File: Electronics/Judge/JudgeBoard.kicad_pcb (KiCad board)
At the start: 2 copper layers, 17 parts, among them J1 RJ12-UNSHLD, U1 74HC165, U2 74HC165

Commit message: UPdated judge board layout
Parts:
- S1: value DPDT-Button -> R1
- S10: value DPDT-Button -> B5
- S2: value DPDT-Button -> R3
- S3: value DPDT-Button -> R5
- S4: value DPDT-Button -> B2
- S5: value DPDT-Button -> B4
- S6: value DPDT-Button -> R2
- S7: value DPDT-Button -> R4
- S8: value DPDT-Button -> B1
- S9: value DPDT-Button -> B3
- moved S6 97.7 mm to (58.9, 81.8)
- moved S7 95.5 mm to (58.4, 115.3)
- moved S4 94.6 mm to (143.3, 81.3)
- moved S5 92.5 mm to (145.8, 115.3)
- moved S9 52.7 mm to (149.4, 95.0)
- moved S1 50.9 mm to (51.3, 105.7)
- moved S2 49.8 mm to (45.2, 96.0)
- moved U2 47.1 mm to (124.5, 106.2), turned to 270 degrees
- moved RN1 42.7 mm to (79.8, 119.9), turned to 0 degrees
- moved S3 30.5 mm to (55.9, 95.0)
- moved S8 29.3 mm to (141.7, 105.2)
- moved S10 23.2 mm to (135.6, 95.0)
- moved J1 14.5 mm to (96.5, 81.3)
- moved C1 10.8 mm to (73.7, 110.7), turned to 90 degrees
- moved C2 9.16 mm to (101.6, 110.7), turned to 90 degrees
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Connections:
- J1 pad 5: Net-(J1-Pad5) -> (no net)
- S1 pad 3: Net-(S1-Pad3) -> (no net)
- S1 pad 4: Net-(S1-Pad4) -> (no net)
- S1 pad 5: Net-(S1-Pad5) -> (no net)
- S1 pad 6: Net-(S1-Pad6) -> (no net)
- S10 pad 3: Net-(S10-Pad3) -> (no net)
- S10 pad 4: Net-(S10-Pad4) -> (no net)
- S10 pad 5: Net-(S10-Pad5) -> (no net)
- S10 pad 6: Net-(S10-Pad6) -> (no net)
- S2 pad 3: Net-(S2-Pad3) -> (no net)
- S2 pad 4: Net-(S2-Pad4) -> (no net)
- S2 pad 5: Net-(S2-Pad5) -> (no net)
- S2 pad 6: Net-(S2-Pad6) -> (no net)
- S3 pad 3: Net-(S3-Pad3) -> (no net)
- S3 pad 4: Net-(S3-Pad4) -> (no net)
- S3 pad 5: Net-(S3-Pad5) -> (no net)
- S3 pad 6: Net-(S3-Pad6) -> (no net)
- S4 pad 3: Net-(S4-Pad3) -> (no net)
- S4 pad 4: Net-(S4-Pad4) -> (no net)
- S4 pad 5: Net-(S4-Pad5) -> (no net)
- S4 pad 6: Net-(S4-Pad6) -> (no net)
- S5 pad 3: Net-(S5-Pad3) -> (no net)
- S5 pad 4: Net-(S5-Pad4) -> (no net)
- S5 pad 5: Net-(S5-Pad5) -> (no net)
- S5 pad 6: Net-(S5-Pad6) -> (no net)
- S6 pad 3: Net-(S6-Pad3) -> (no net)
- S6 pad 4: Net-(S6-Pad4) -> (no net)
- S6 pad 5: Net-(S6-Pad5) -> (no net)
- S6 pad 6: Net-(S6-Pad6) -> (no net)
- S7 pad 3: Net-(S7-Pad3) -> (no net)
- S7 pad 4: Net-(S7-Pad4) -> (no net)
- S7 pad 5: Net-(S7-Pad5) -> (no net)
- S7 pad 6: Net-(S7-Pad6) -> (no net)
- S8 pad 3: Net-(S8-Pad3) -> (no net)
- S8 pad 4: Net-(S8-Pad4) -> (no net)
- S8 pad 5: Net-(S8-Pad5) -> (no net)
- S8 pad 6: Net-(S8-Pad6) -> (no net)
- S9 pad 3: Net-(S9-Pad3) -> (no net)
- S9 pad 4: Net-(S9-Pad4) -> (no net)
- S9 pad 5: Net-(S9-Pad5) -> (no net)
- S9 pad 6: Net-(S9-Pad6) -> (no net)
- U1 pad 7: Net-(U1-Pad7) -> (no net)
- U2 pad 7: Net-(U2-Pad7) -> (no net)
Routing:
- net GND: track 0.00 -> 141.2 mm
- net Net-(RN1-Pad3): track 0.00 -> 103.4 mm
- net Net-(RN1-Pad4): track 0.00 -> 53.3 mm
- net Net-(RN1-Pad2): track 0.00 -> 42.1 mm
- net Net-(RN1-Pad5): track 0.00 -> 39.8 mm
- net Net-(RN1-Pad6): track 0.00 -> 35.9 mm
- net Net-(RN1-Pad9): track 0.00 -> 27.2 mm
- net +3V3: track 0.00 -> 14.9 mm

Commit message: Controller design iteration, code refactoring modifications
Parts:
- moved S7 22.7 mm to (36.6, 109.2)
- moved S1 20.0 mm to (44.5, 124.5)
- moved S3 14.0 mm to (54.9, 109.0)
- moved S2 2.50 mm to (47.5, 97.0)
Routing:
- net GND: track 141.2 -> 267.1 mm
- net Net-(RN1-Pad3): track 103.4 -> 6.52 mm
- net Net-(RN1-Pad8): track 0.00 -> 90.4 mm
- net Net-(RN1-Pad9): track 27.2 -> 109.3 mm
- net Net-(RN1-Pad10): track 0.00 -> 59.7 mm
- net Net-(RN1-Pad11): track 0.00 -> 54.2 mm
- net Net-(RN1-Pad4): track 53.3 -> 6.52 mm
- net Net-(RN1-Pad6): track 35.9 -> 0.00 mm
- net Net-(RN1-Pad5): track 39.8 -> 6.52 mm
- net /LOAD: track 0.00 -> 26.2 mm
- net +3V3: track 14.9 -> 24.5 mm
- net Net-(RN1-Pad2): track 42.1 -> 45.0 mm

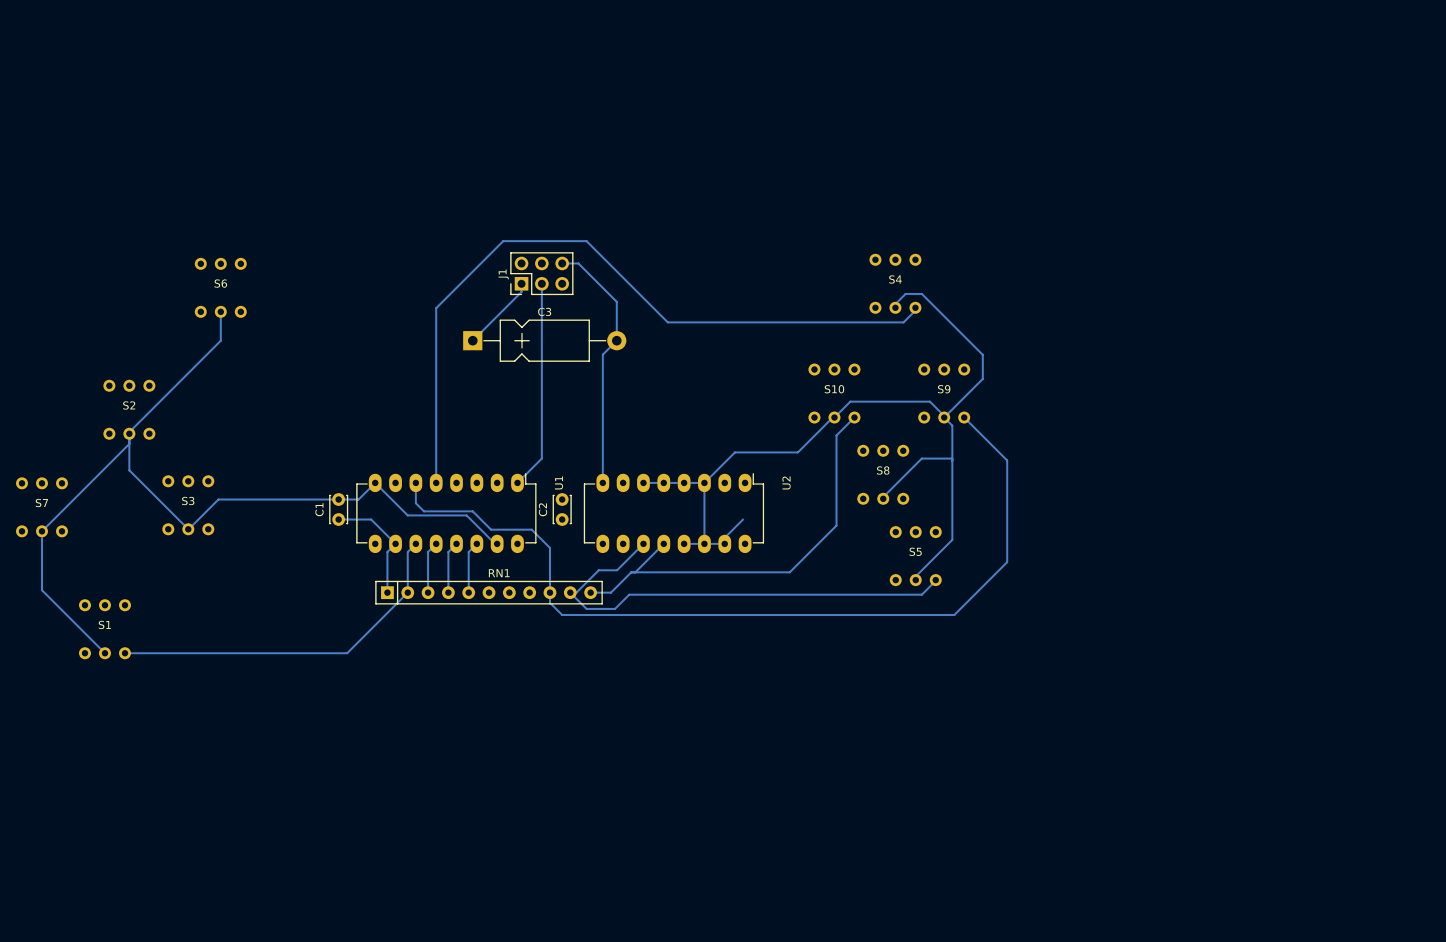
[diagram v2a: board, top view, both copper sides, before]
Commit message: Simplified judge controller schematic and pcb
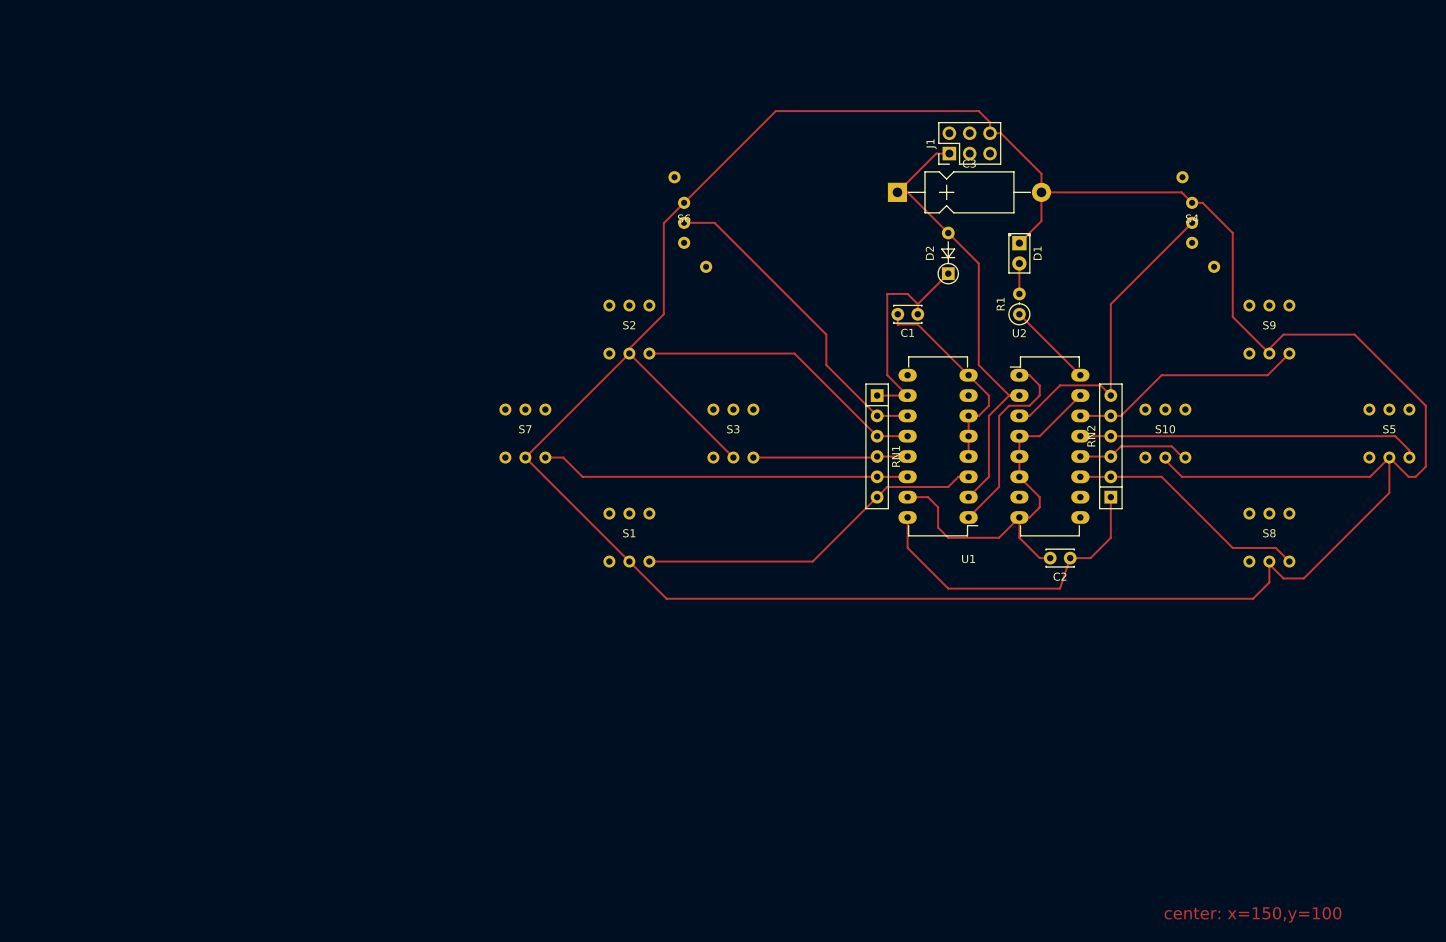
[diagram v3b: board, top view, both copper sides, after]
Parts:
- added D1: LED, LEDs:LED_D2.0mm_W4.8mm_H2.5mm_FlatTop, F.Cu at (158.8, 76.2)
- added D2: D, Diodes_THT:D_DO-35_SOD27_P5.08mm_Vertical_AnodeUp, F.Cu at (149.9, 80.0)
- added R1: R, Resistors_THT:R_Axial_DIN0207_L6.3mm_D2.5mm_P2.54mm_Vertical, F.Cu at (158.8, 85.1)
- added RN2: R_Network05, Resistors_THT:R_Array_SIP6, F.Cu at (170.2, 108.0)
- RN1: value R_Network10 -> R_Network05; footprint Resistors_THT:Resistor_Array_SIP11 -> Resistors_THT:R_Array_SIP6
- S4, S6: footprint Buttons_Switches_THT:MHPS2285V -> PiKwonDo:Switch-SPDT
- moved C1 76.8 mm to (146.1, 85.1), turned to 180 degrees
- moved S3 68.7 mm to (123.0, 100.0)
- moved S1 66.5 mm to (110.0, 113.0)
- moved RN1 66.0 mm to (141.0, 95.2), turned to 270 degrees
- moved C2 63.7 mm to (165.1, 115.6), turned to 180 degrees
- moved S2 63.3 mm to (110.0, 87.0)
- moved S5 61.2 mm to (205.0, 100.0)
- moved S7 61.1 mm to (97.0, 100.0)
- moved S6 58.5 mm to (116.8, 73.7)
- moved U1 56.6 mm to (152.4, 110.5), turned to 180 degrees
- moved C3 56.2 mm to (143.5, 69.8)
- moved J1 55.9 mm to (150.0, 65.0)
- moved S8 48.9 mm to (190.0, 113.0)
- moved S10 41.7 mm to (177.0, 100.0)
- moved S9 41.4 mm to (190.0, 87.0)
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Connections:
- C3 pad 1: +3V3 -> /CLK
- J1 pad 1: +3V3 -> /CLK
- J1 pad 2: /CLK -> /LOAD
- J1 pad 3: /LOAD -> Net-(J1-Pad3)
- J1 pad 5: (no net) -> Net-(J1-Pad5)
- S1 pad 1: Net-(RN1-Pad2) -> Net-(RN1-Pad6)
- S1 pad 3: (no net) -> Net-(S1-Pad3)
- S1 pad 4: (no net) -> Net-(S1-Pad4)
- S1 pad 5: (no net) -> Net-(S1-Pad5)
- S1 pad 6: (no net) -> Net-(S1-Pad6)
- S10 pad 1: Net-(RN1-Pad11) -> Net-(RN2-Pad3)
- S10 pad 3: (no net) -> Net-(S10-Pad3)
- S10 pad 4: (no net) -> Net-(S10-Pad4)
- S10 pad 5: (no net) -> Net-(S10-Pad5)
- S10 pad 6: (no net) -> Net-(S10-Pad6)
- S2 pad 1: Net-(RN1-Pad4) -> Net-(RN1-Pad3)
- S2 pad 3: (no net) -> Net-(S2-Pad3)
- S2 pad 4: (no net) -> Net-(S2-Pad4)
- S2 pad 5: (no net) -> Net-(S2-Pad5)
- S2 pad 6: (no net) -> Net-(S2-Pad6)
- S3 pad 1: Net-(RN1-Pad6) -> Net-(RN1-Pad4)
- S3 pad 3: (no net) -> Net-(S3-Pad3)
- S3 pad 4: (no net) -> Net-(S3-Pad4)
- S3 pad 5: (no net) -> Net-(S3-Pad5)
- S3 pad 6: (no net) -> Net-(S3-Pad6)
- S4 pad 1: Net-(RN1-Pad8) -> Net-(RN2-Pad6)
- S4 pad 3: (no net) -> Net-(S4-Pad3)
- S5 pad 1: Net-(RN1-Pad10) -> Net-(RN2-Pad4)
- S5 pad 3: (no net) -> Net-(S5-Pad3)
- S5 pad 4: (no net) -> Net-(S5-Pad4)
- S5 pad 5: (no net) -> Net-(S5-Pad5)
- S5 pad 6: (no net) -> Net-(S5-Pad6)
- S6 pad 1: Net-(RN1-Pad3) -> Net-(RN1-Pad2)
- S6 pad 3: (no net) -> Net-(S6-Pad3)
- S7 pad 3: (no net) -> Net-(S7-Pad3)
- S7 pad 4: (no net) -> Net-(S7-Pad4)
- S7 pad 5: (no net) -> Net-(S7-Pad5)
- S7 pad 6: (no net) -> Net-(S7-Pad6)
- S8 pad 1: Net-(RN1-Pad7) -> Net-(RN2-Pad2)
- S8 pad 3: (no net) -> Net-(S8-Pad3)
- S8 pad 4: (no net) -> Net-(S8-Pad4)
- S8 pad 5: (no net) -> Net-(S8-Pad5)
- S8 pad 6: (no net) -> Net-(S8-Pad6)
- S9 pad 1: Net-(RN1-Pad9) -> Net-(RN2-Pad5)
- S9 pad 3: (no net) -> Net-(S9-Pad3)
- S9 pad 4: (no net) -> Net-(S9-Pad4)
- S9 pad 5: (no net) -> Net-(S9-Pad5)
- S9 pad 6: (no net) -> Net-(S9-Pad6)
- U1 pad 4: Net-(RN1-Pad7) -> GND
- U1 pad 5: Net-(RN1-Pad8) -> GND
- U1 pad 6: Net-(RN1-Pad9) -> GND
- U1 pad 7: (no net) -> Net-(U1-Pad7)
- U2 pad 11: Net-(RN1-Pad10) -> Net-(RN2-Pad2)
- U2 pad 12: Net-(RN1-Pad11) -> Net-(RN2-Pad3)
- U2 pad 13: GND -> Net-(RN2-Pad4)
- U2 pad 14: GND -> Net-(RN2-Pad5)
- U2 pad 3: GND -> Net-(RN2-Pad6)
- U2 pad 7: (no net) -> Net-(U2-Pad7)
- U2 pad 9: Net-(J1-Pad4) -> Net-(J1-Pad3)
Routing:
- net GND: track 267.1 -> 437.1 mm
- net Net-(RN1-Pad9): track 109.3 -> 0.00 mm
- net Net-(RN1-Pad8): track 90.4 -> 0.00 mm
- net Net-(RN1-Pad10): track 59.7 -> 0.00 mm
- net /CLK: track 0.00 -> 57.8 mm
- net +3V3: track 24.5 -> 79.5 mm
- net Net-(RN1-Pad11): track 54.2 -> 0.00 mm
- net Net-(RN1-Pad6): track 0.00 -> 44.3 mm
- net Net-(RN2-Pad4): track 0.00 -> 42.8 mm
- net Net-(RN1-Pad5): track 6.52 -> 46.3 mm
- net Net-(RN2-Pad6): track 0.00 -> 39.3 mm
- net Net-(RN2-Pad2): track 0.00 -> 30.5 mm
- net Net-(RN1-Pad3): track 6.52 -> 36.6 mm
- net Net-(RN2-Pad5): track 0.00 -> 29.4 mm
- net Net-(RN2-Pad3): track 0.00 -> 14.2 mm
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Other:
- board text added: "center: x=150,y=100"

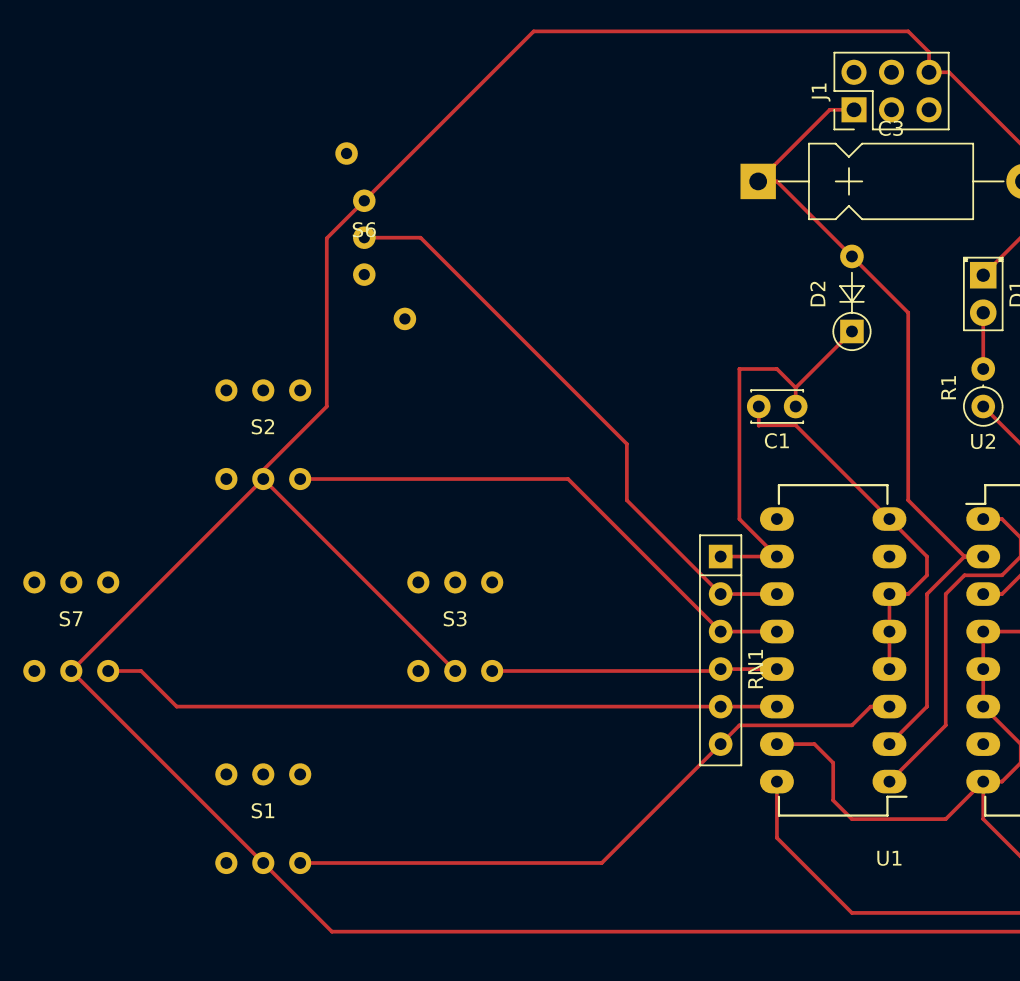
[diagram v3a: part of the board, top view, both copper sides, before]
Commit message: Updated trace locations
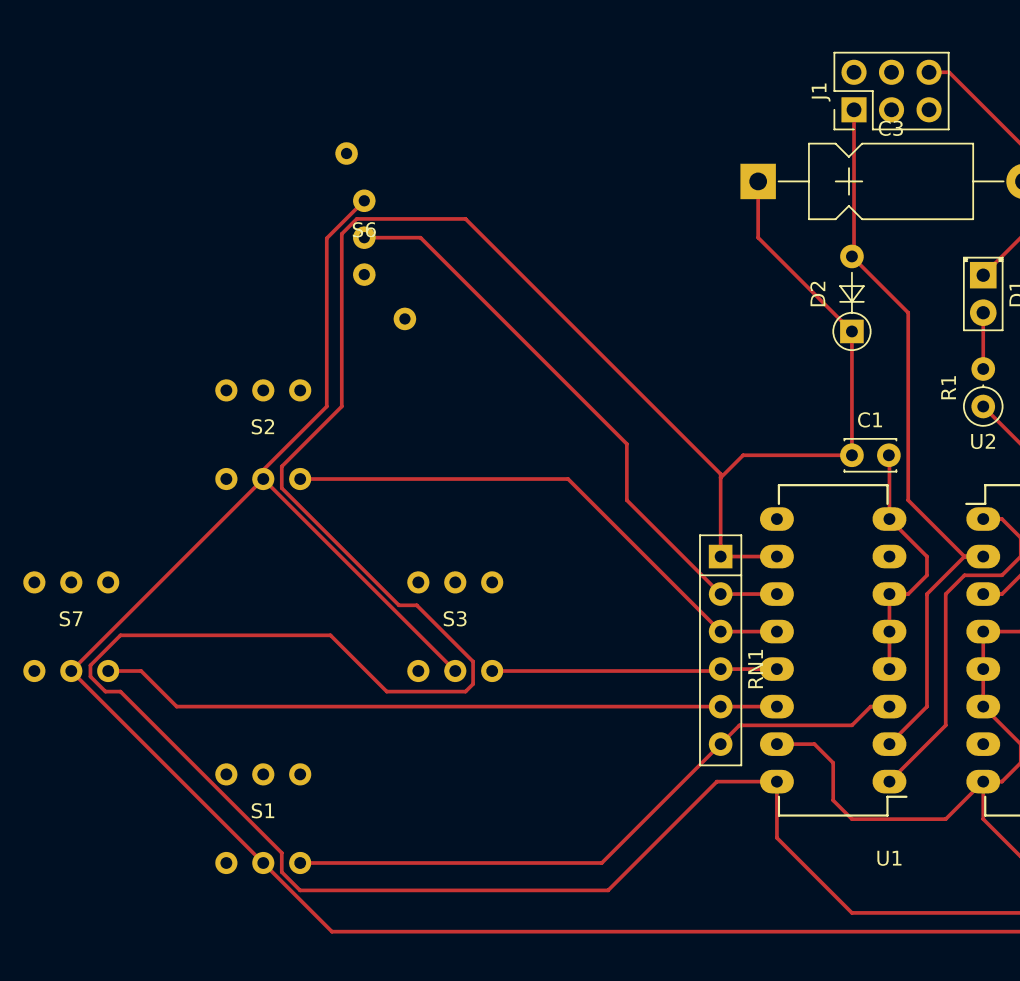
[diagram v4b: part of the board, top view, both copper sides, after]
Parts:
- moved C1 5.04 mm to (149.9, 88.4), turned to 0 degrees
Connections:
- C3 pad 1: /CLK -> +3V3
- J1 pad 4: Net-(J1-Pad4) -> (no net)
- J1 pad 5: Net-(J1-Pad5) -> (no net)
- S1 pad 3: Net-(S1-Pad3) -> (no net)
- S1 pad 4: Net-(S1-Pad4) -> (no net)
- S1 pad 5: Net-(S1-Pad5) -> (no net)
- S1 pad 6: Net-(S1-Pad6) -> (no net)
- S10 pad 3: Net-(S10-Pad3) -> (no net)
- S10 pad 4: Net-(S10-Pad4) -> (no net)
- S10 pad 5: Net-(S10-Pad5) -> (no net)
- S10 pad 6: Net-(S10-Pad6) -> (no net)
- S2 pad 3: Net-(S2-Pad3) -> (no net)
- S2 pad 4: Net-(S2-Pad4) -> (no net)
- S2 pad 5: Net-(S2-Pad5) -> (no net)
- S2 pad 6: Net-(S2-Pad6) -> (no net)
- S3 pad 3: Net-(S3-Pad3) -> (no net)
- S3 pad 4: Net-(S3-Pad4) -> (no net)
- S3 pad 5: Net-(S3-Pad5) -> (no net)
- S3 pad 6: Net-(S3-Pad6) -> (no net)
- S4 pad 3: Net-(S4-Pad3) -> (no net)
- S5 pad 3: Net-(S5-Pad3) -> (no net)
- S5 pad 4: Net-(S5-Pad4) -> (no net)
- S5 pad 5: Net-(S5-Pad5) -> (no net)
- S5 pad 6: Net-(S5-Pad6) -> (no net)
- S6 pad 3: Net-(S6-Pad3) -> (no net)
- S7 pad 3: Net-(S7-Pad3) -> (no net)
- S7 pad 4: Net-(S7-Pad4) -> (no net)
- S7 pad 5: Net-(S7-Pad5) -> (no net)
- S7 pad 6: Net-(S7-Pad6) -> (no net)
- S8 pad 3: Net-(S8-Pad3) -> (no net)
- S8 pad 4: Net-(S8-Pad4) -> (no net)
- S8 pad 5: Net-(S8-Pad5) -> (no net)
- S8 pad 6: Net-(S8-Pad6) -> (no net)
- S9 pad 3: Net-(S9-Pad3) -> (no net)
- S9 pad 4: Net-(S9-Pad4) -> (no net)
- S9 pad 5: Net-(S9-Pad5) -> (no net)
- S9 pad 6: Net-(S9-Pad6) -> (no net)
- U1 pad 7: Net-(U1-Pad7) -> (no net)
- U2 pad 7: Net-(U2-Pad7) -> (no net)
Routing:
- net +3V3: track 79.5 -> 248.1 mm
- net GND: track 437.1 -> 383.7 mm
- net /CLK: track 57.8 -> 50.8 mm
